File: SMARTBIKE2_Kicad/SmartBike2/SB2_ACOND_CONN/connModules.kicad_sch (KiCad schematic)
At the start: 4 parts, among them J3 Conn_01x05, J4 Conn_01x06, J5 Conn_01x08, J6 Conn_01x04

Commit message: Fase 2 de 3 panel full
+ PCB Acondicionamiento y Módulos

~ Esquemático Luces
~ PCB 3 de 3, Luces
~ Panelización
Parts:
- removed J4: Conn_01x06, Connector_PinSocket_2.54mm:PinSocket_1x06_P2.54mm_Vertical, symbol Connector_Generic:Conn_01x06
- added J6: Conn_01x08, Connector_PinHeader_2.54mm:PinHeader_1x08_P2.54mm_Vertical, symbol Connector_Generic:Conn_01x08
- renumbered J5 to J?, J6 to J?, J3 to J?
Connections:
- net 4.1V: now also J6.1 (Pin_1)
- net GND: now also J6.2 (Pin_2), J6.8 (Pin_8)
- net RstSIM: now also J6.7 (Pin_7)
- net RxSIM: now also J6.3 (Pin_3)
- net TxSIM: now also J6.4 (Pin_4)
- new net NE: J6.5 (Pin_5)
- new net VDO_SIM: J6.6 (Pin_6)
- no-connect marks 10 -> 4
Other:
- note added: "EL conector de la izq es pensado para la SIM800L, mientras que el de la derecha para SIMA7670AS. Por ello, se debe tener cuidado en la programación con el pin "RST", ya que pueden tener diferente función para cada módulo. Para el módulo SIMA7670AS el nombre de "RST" es PWR_EN."
- moved on the sheet: J?

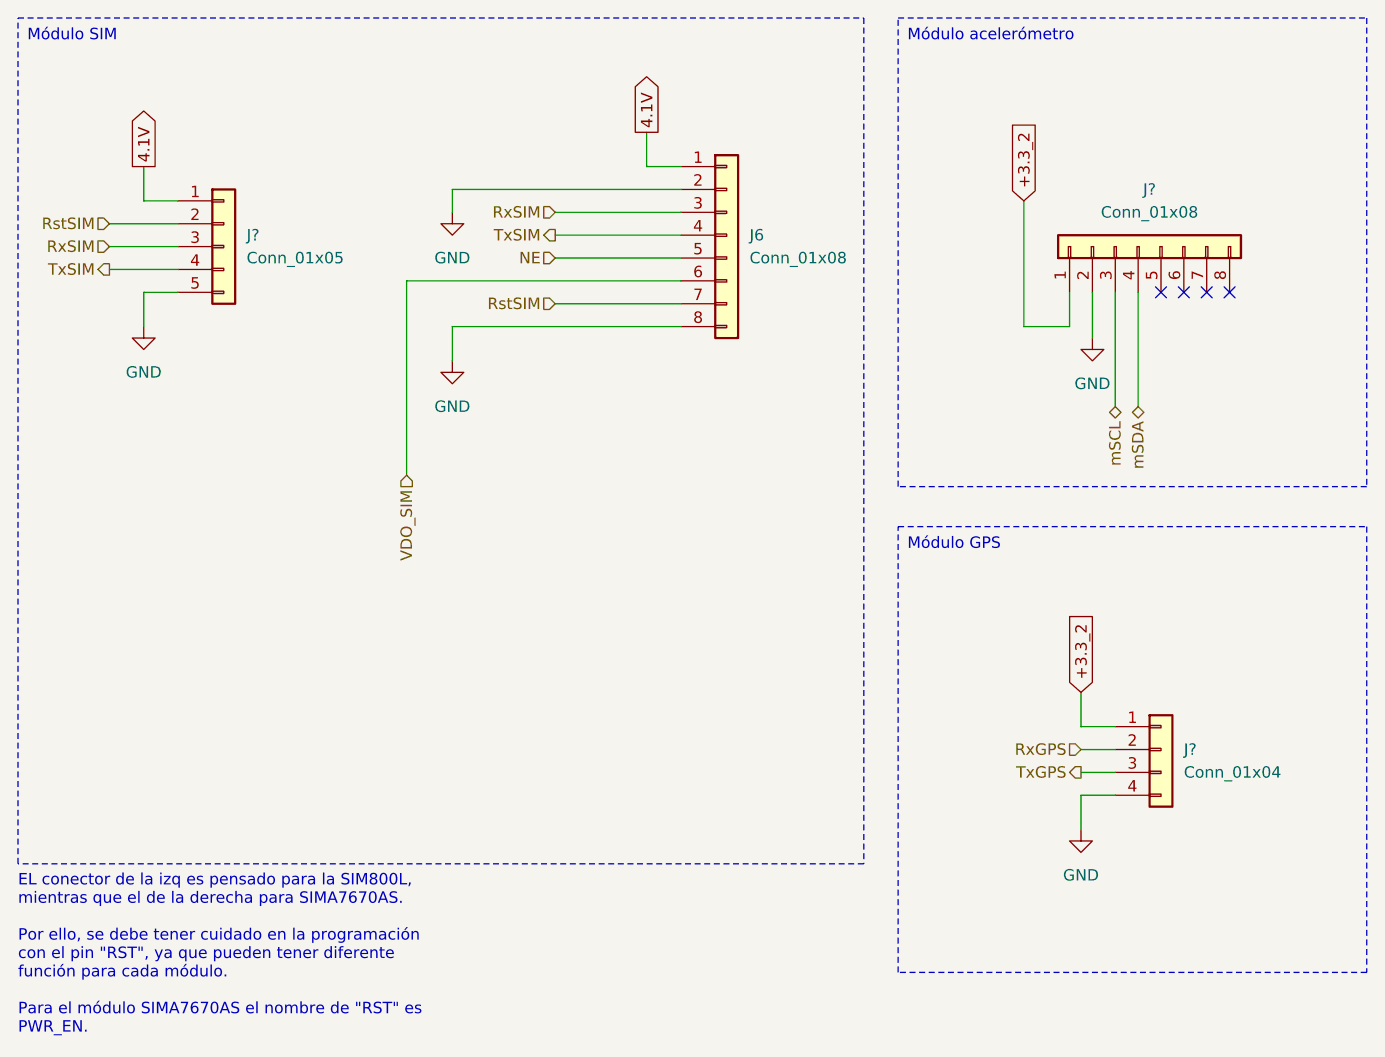
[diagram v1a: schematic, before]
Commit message: Impresión vías sin metalización
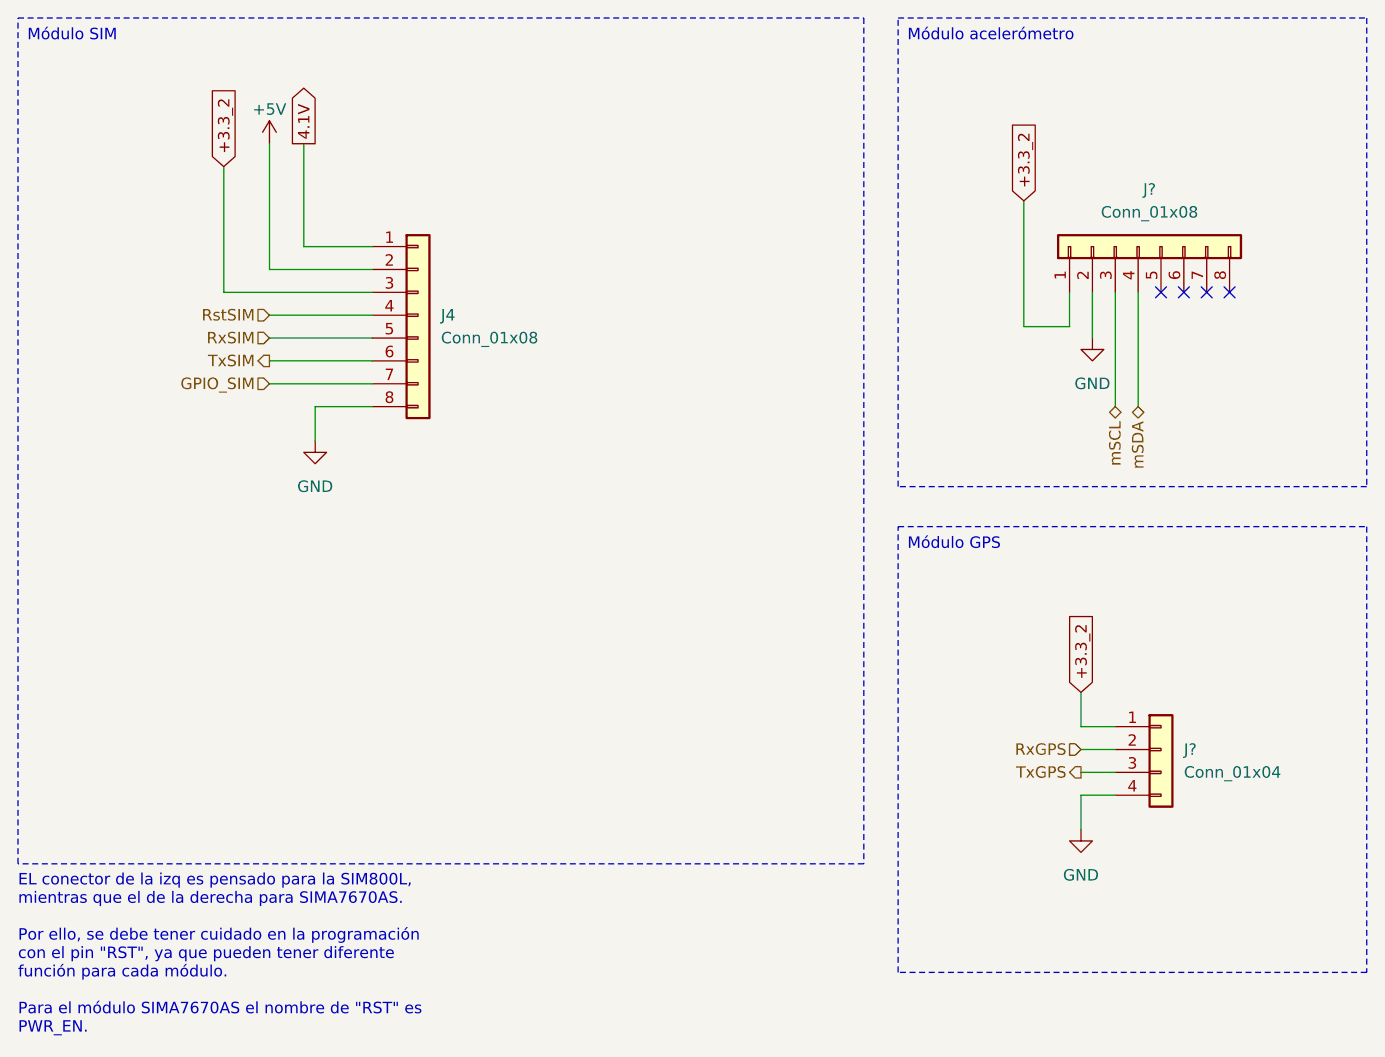
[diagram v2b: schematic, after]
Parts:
- removed J6: Conn_01x08, Connector_PinHeader_2.54mm:PinHeader_1x08_P2.54mm_Vertical, symbol Connector_Generic:Conn_01x08
- removed J?: Conn_01x05, Connector_PinSocket_2.54mm:PinSocket_1x05_P2.54mm_Vertical, symbol Connector_Generic:Conn_01x05
- added J4: Conn_01x08, Connector_PinHeader_2.54mm:PinHeader_1x08_P2.54mm_Vertical, symbol Connector_Generic:Conn_01x08
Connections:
- net +3.3_2: now also J4.3 (Pin_3)
- net 4.1V: now also J4.1 (Pin_1)
- net GND: now also J4.8 (Pin_8)
- net RstSIM: now also J4.4 (Pin_4)
- net RxSIM: now also J4.5 (Pin_5)
- net TxSIM: now also J4.6 (Pin_6)
- new net +5V: J4.2 (Pin_2)
- new net GPIO_SIM: J4.7 (Pin_7)

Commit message: Cambios Finales
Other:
- note added: "Pines de propósito general compatibles con diversos módulos SIM. Estos pines deben ser conectados manualmente con cables."
- note removed: "EL conector de la izq es pensado para la SIM800L, mientras que el de la derecha para SIMA7670AS. Por ello, se debe tener cuidado en la programación con el pin "RST", ya que pueden tener diferente función para cada módulo. Para el módulo SIMA7670AS el nombre de "RST" es PWR_EN."
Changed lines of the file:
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@@
     (effects (font (size 1.27 1.27)) (justify left top))
   )
-  (text "EL conector de la izq es pensado para la SIM800L, \nmientras que el de la derecha para SIMA7670AS.\n\nPor ello, se debe tener cuidado en la programación\ncon el pin \"RST\", ya que pueden tener diferente \nfunción para cada módulo.\n\nPara el módulo SIMA7670AS el nombre de \"RST\" es \nPWR_EN."
-    (at 15.24 147.32 0)
+  (text "Pines de propósito general compatibles con diversos módulos SIM.\n\nEstos pines deben ser conectados manualmente con cables."
+    (at 15.24 135.89 0)
     (effects (font (size 1.27 1.27)) (justify left bottom))
   )
